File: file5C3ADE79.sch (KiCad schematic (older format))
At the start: 118 parts

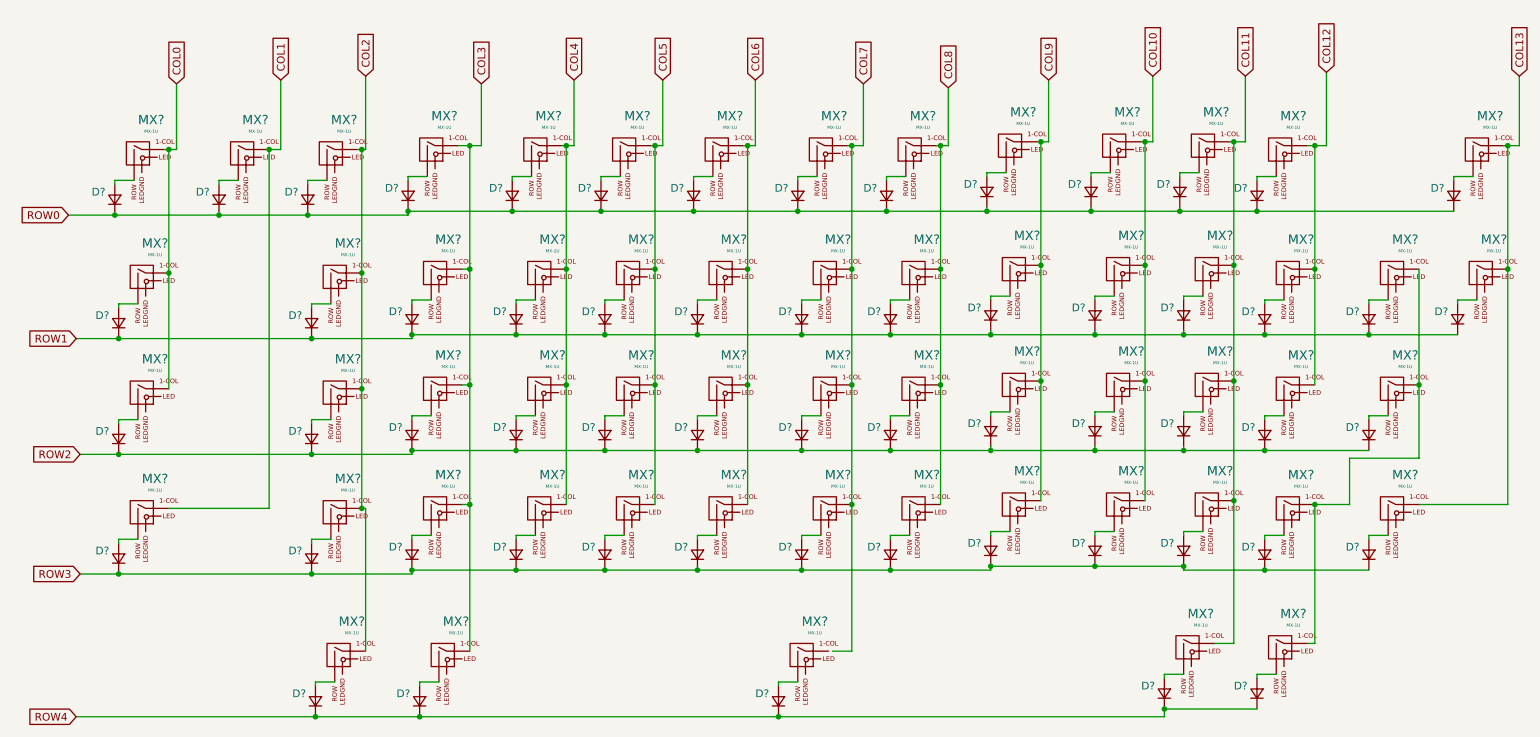
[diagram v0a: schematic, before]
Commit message: Added Submodules
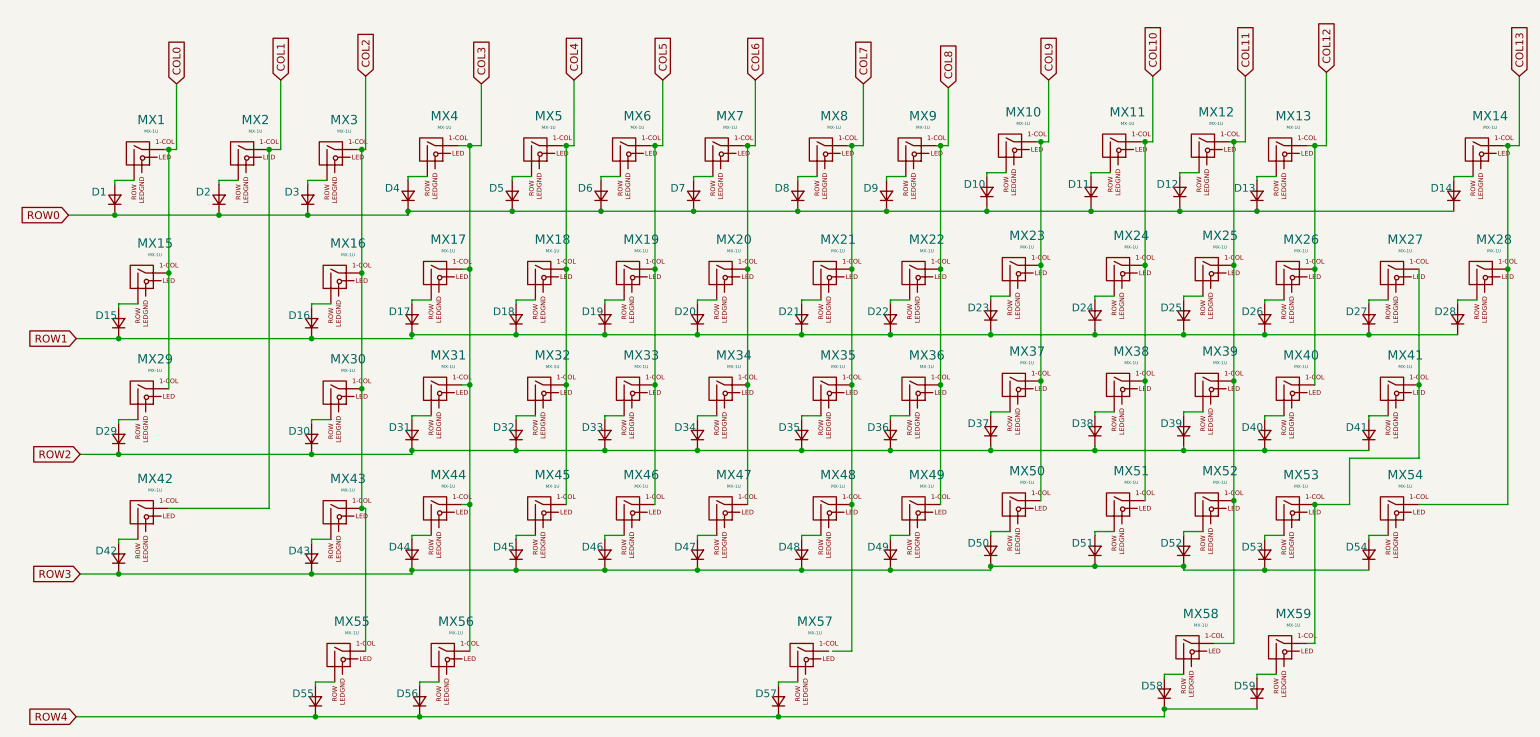
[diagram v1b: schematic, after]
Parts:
- gave numbers to parts that had none: 118

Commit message: Generated Netlist
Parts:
- removed MX14, MX15, MX28, MX29, MX41, MX42, MX53, MX56, MX57, MX58: MX-1U, symbol MX_Alps_Hybrids:MX-1U
- added MX14, MX41: MX-2U, symbol MX_Alps_Hybrids:MX-2U
- added MX15, MX28, MX56, MX58: MX-1.5U, symbol MX_Alps_Hybrids:MX-1.5U
- added MX29, MX53: MX-1.75U, symbol MX_Alps_Hybrids:MX-1.75U
- added MX42: MX-2.25U, symbol MX_Alps_Hybrids:MX-2.25U
- added MX57: MX-7U, symbol MX_Alps_Hybrids:MX-7U
- D1, D10, D11, D12, D13, D14, D15, D16, D17, D18, D19, D2, D20, D21, D22, D23, D24, D25, D26, D27, D28, D29, D3, D30, D31, D32, D33, D34, D35, D36, D37, D38, D39, D4, D40, D41, D42, D43, D44, D45, D46, D47, D48, D49, D5, D50, D51, D52, D53, D54, D55, D56, D57, D58, D59, D6, D7, D8, D9: footprint (none) -> Diode_SMD:D_SOD-123
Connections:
- net COL0: now also MX15.1 (COL), MX29.1 (COL)
- net COL1: now also MX42.1 (COL)
- net COL11: now also MX58.1 (COL)
- net COL13: now also MX14.1 (COL), MX28.1 (COL)
- net COL3: now also MX56.1 (COL)
- net at D14.2 (A): now also MX14.2 (ROW)
- net at D15.2 (A): now also MX15.2 (ROW)
- net at MX27.1 (COL), MX59.1 (COL): now also MX41.1 (COL), MX53.1 (COL)
- net at D28.2 (A): now also MX28.2 (ROW)
- net at D29.2 (A): now also MX29.2 (ROW)
- net at D41.2 (A): now also MX41.2 (ROW)
- net at D42.2 (A): now also MX42.2 (ROW)
- net at D53.2 (A): now also MX53.2 (ROW)
- net at D56.2 (A): now also MX56.2 (ROW)
- net at D57.2 (A): now also MX57.2 (ROW)
- net at D58.2 (A): now also MX58.2 (ROW)

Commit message: PCB Layout done
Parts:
- D1: value D_Small -> D
- MX1, MX10, MX11, MX12, MX13, MX14, MX15, MX16, MX17, MX18, MX19, MX2, MX20, MX21, MX22, MX23, MX24, MX25, MX26, MX27, MX28, MX29, MX3, MX30, MX31, MX32, MX33, MX34, MX35, MX36, MX37, MX38, MX39, MX4, MX40, MX41, MX42, MX43, MX44, MX45, MX46, MX47, MX48, MX49, MX5, MX50, MX51, MX52, MX53, MX54, MX55, MX56, MX57, MX58, MX59, MX6, MX7, MX8, MX9: footprint (none) -> keyboard_parts:Kailh_MX_Socket_LED

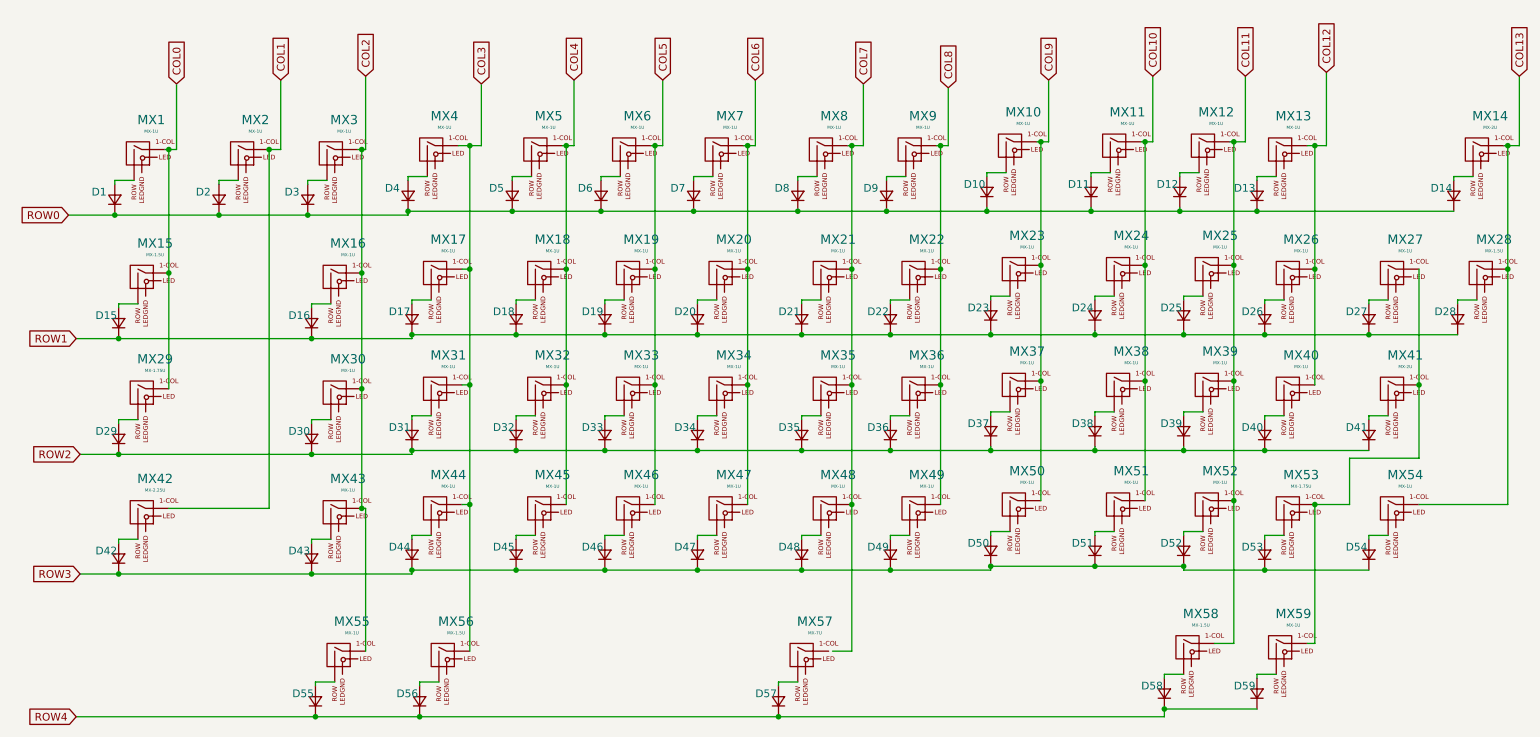
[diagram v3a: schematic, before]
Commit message: Added type C
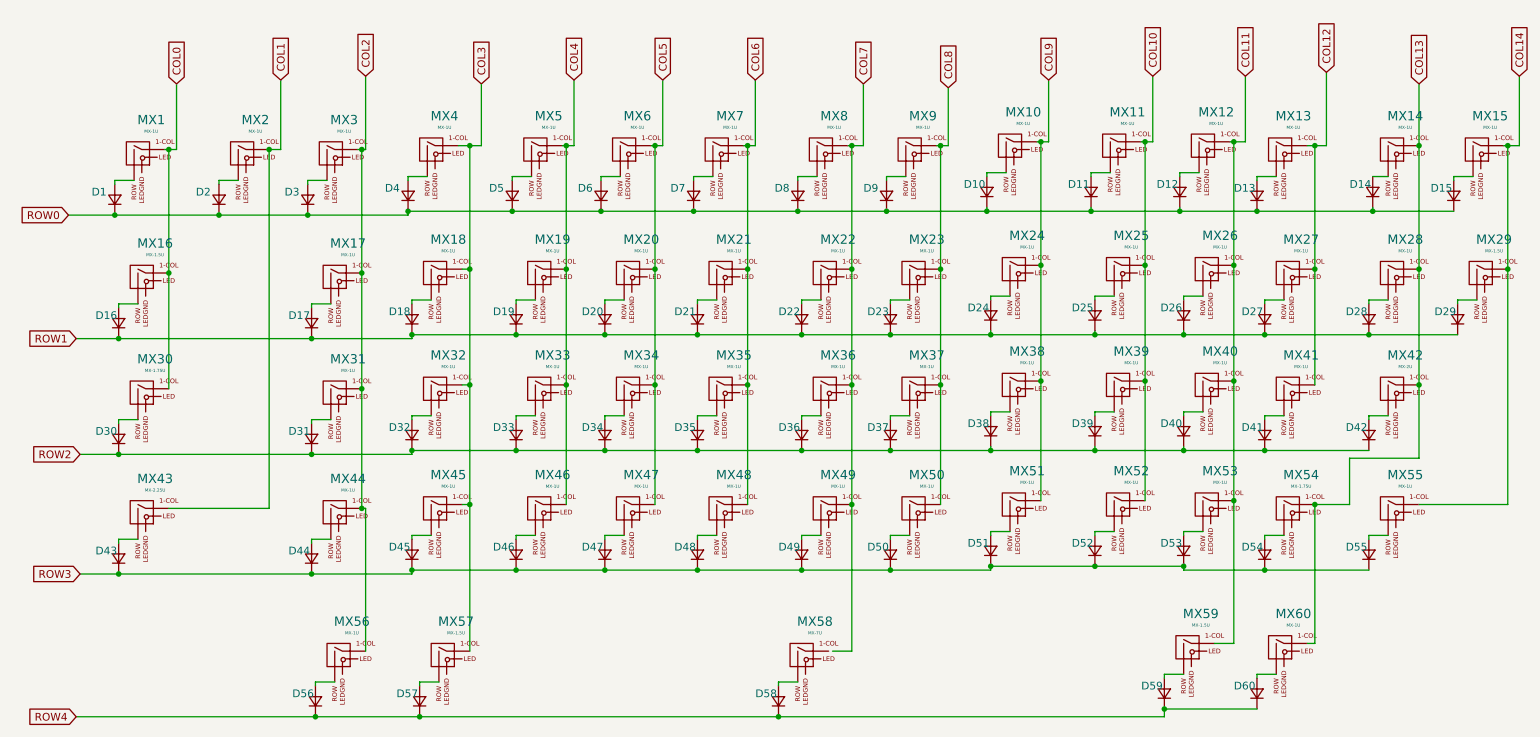
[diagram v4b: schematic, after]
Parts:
- removed MX14: MX-2U, keyboard_parts:Kailh_MX_Socket_LED, symbol MX_Alps_Hybrids:MX-2U
- added D14: D_Small, Diode_SMD:D_SOD-123, symbol Device:D_Small
- added MX14, MX15: MX-1U, keyboard_parts:Kailh_MX_Socket_LED, symbol MX_Alps_Hybrids:MX-1U
- renumbered D14 to D15, D15 to D16, D16 to D17, D17 to D18, D18 to D19, D19 to D20, D20 to D21, D21 to D22, D22 to D23, D23 to D24, D24 to D25, D25 to D26, D26 to D27, D27 to D28, D28 to D29, D29 to D30, D30 to D31, D31 to D32, D32 to D33, D33 to D34, D34 to D35, D35 to D36, D36 to D37, D37 to D38, D38 to D39, D39 to D40, D40 to D41, D41 to D42, D42 to D43, D43 to D44, D44 to D45, D45 to D46, D46 to D47, D47 to D48, D48 to D49, D49 to D50, D50 to D51, D51 to D52, D52 to D53, D53 to D54, D54 to D55, D55 to D56, D56 to D57, D57 to D58, D58 to D59, D59 to D60, MX15 to MX16, MX16 to MX17, MX17 to MX18, MX18 to MX19, MX19 to MX20, MX20 to MX21, MX21 to MX22, MX22 to MX23, MX23 to MX24, MX24 to MX25, MX25 to MX26, MX26 to MX27, MX27 to MX28, MX28 to MX29, MX29 to MX30, MX30 to MX31, MX31 to MX32, MX32 to MX33, MX33 to MX34, MX34 to MX35, MX35 to MX36, MX36 to MX37, MX37 to MX38, MX38 to MX39, MX39 to MX40, MX40 to MX41, MX41 to MX42, MX42 to MX43, MX43 to MX44, MX44 to MX45, MX45 to MX46, MX46 to MX47, MX47 to MX48, MX48 to MX49, MX49 to MX50, MX50 to MX51, MX51 to MX52, MX52 to MX53, MX53 to MX54, MX54 to MX55, MX55 to MX56, MX56 to MX57, MX57 to MX58, MX58 to MX59, MX59 to MX60
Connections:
- net COL13: now also MX28.1 (COL), MX42.1 (COL), MX54.1 (COL), MX60.1 (COL), MX14.1 (COL); no longer MX29.1 (COL), MX55.1 (COL)
- net ROW0: now also D14.1 (K)
- net at D15.2 (A): now also MX15.2 (ROW)
- new net: D14.2 (A), MX14.2 (ROW)
- new net COL14: MX15.1 (COL), MX29.1 (COL), MX55.1 (COL)

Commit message: Routed all cols
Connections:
- net COL7: now also MX58.1 (COL)
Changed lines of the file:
@@
 Wire Wire Line
 	5375 1650 5400 1650
-Wire Wire Line
-	6550 4925 6675 4925
 Connection ~ 4825 1650
 Wire Wire Line
@@
 Text GLabel 1675 4425 0    50   Input ~ 0
 ROW3
+Wire Wire Line
+	6525 4925 6675 4925
 $EndSCHEMATC
